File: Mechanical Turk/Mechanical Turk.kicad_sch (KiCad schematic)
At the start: 6 parts, among them J1 Conn_01x01_Pin

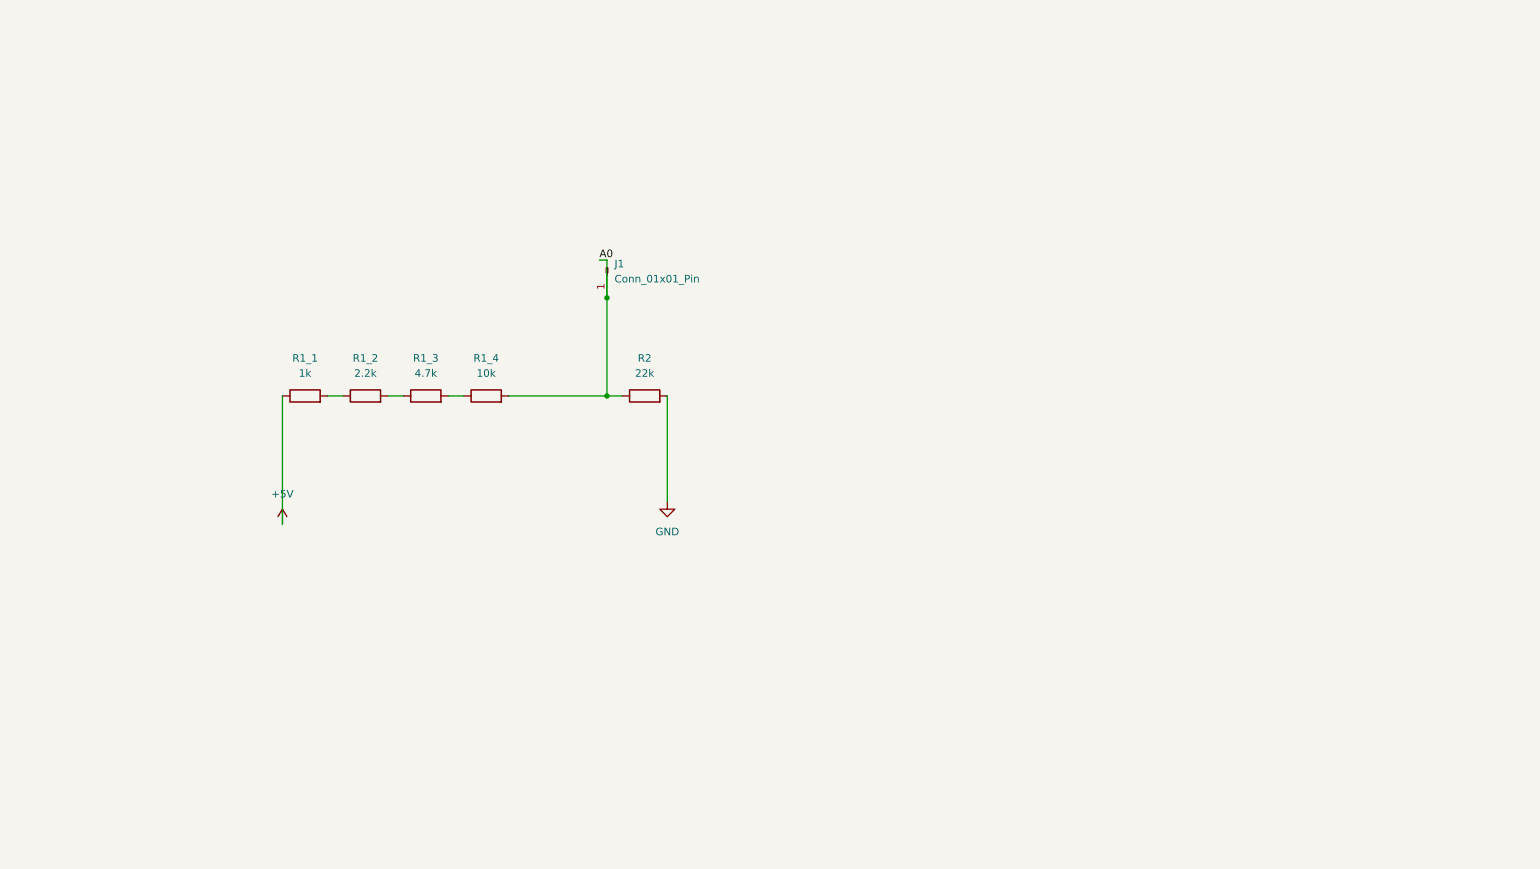
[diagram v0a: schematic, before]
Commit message: code now works better. before ti was reading the analog pins one by one so it was taking about two seconds to get a reading. now it takes 1/16th of that.
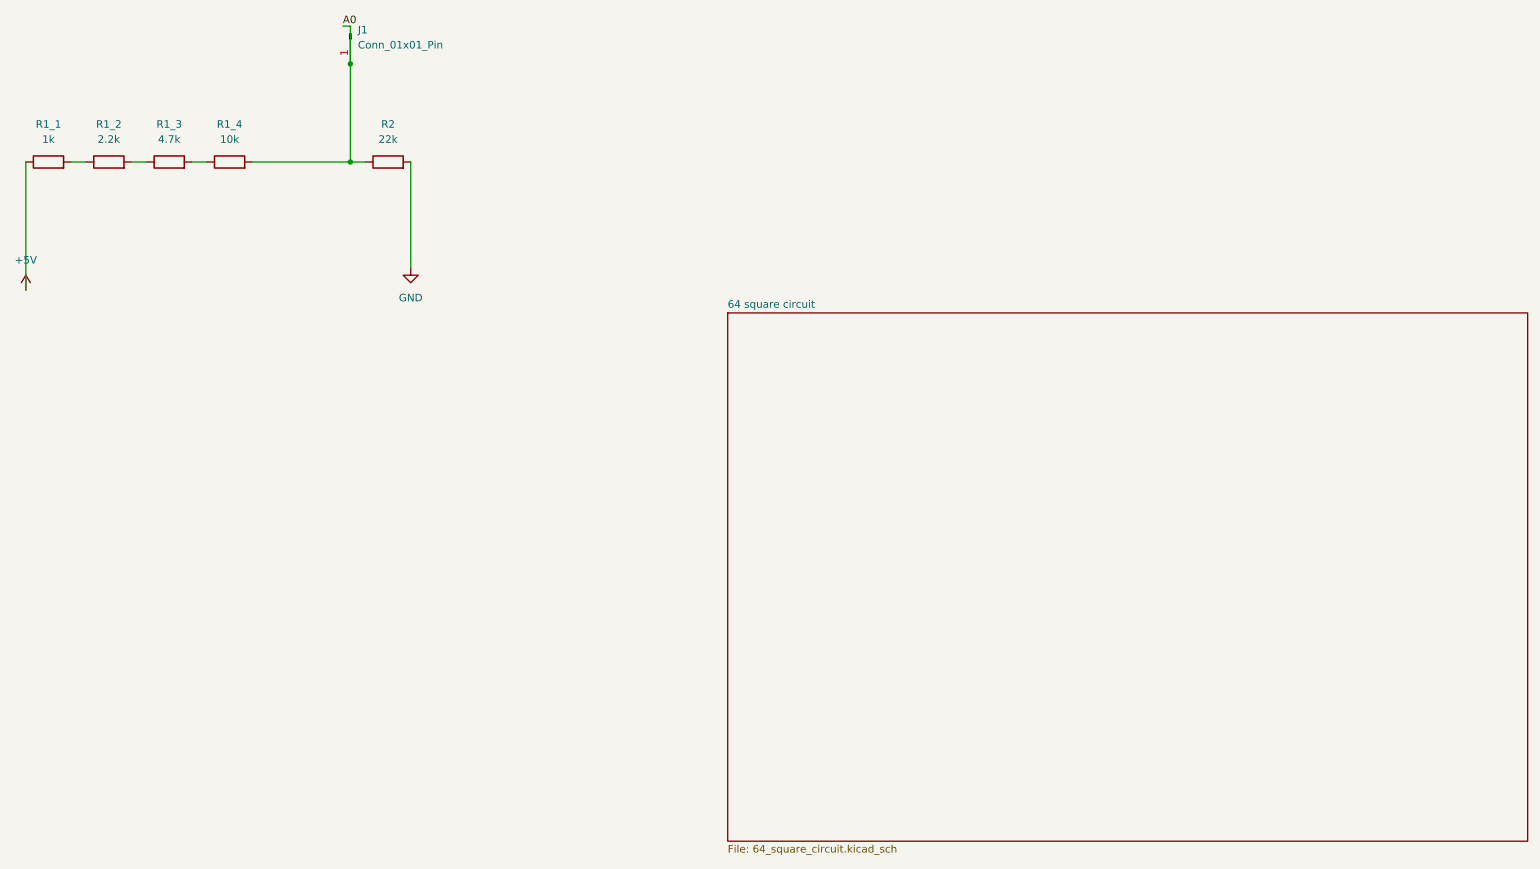
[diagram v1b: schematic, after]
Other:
- added sheet 64 square circuit (64_square_circuit.kicad_sch)
- moved on the sheet: J1, R1_1, R1_2, R1_3, R1_4, R2
